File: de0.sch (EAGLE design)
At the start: 154 parts, among them IC1 PL2303SA__LF, J2 UX60SC-MB-5ST, Q1 BSH103,235, Q2 BSH103,235, Q3 BSH103,235, Q4 BSH103,235, Q5 BSH103,235, SW0 SS12SDP2, SW1 SS12SDP2, SW2 SS12SDP2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

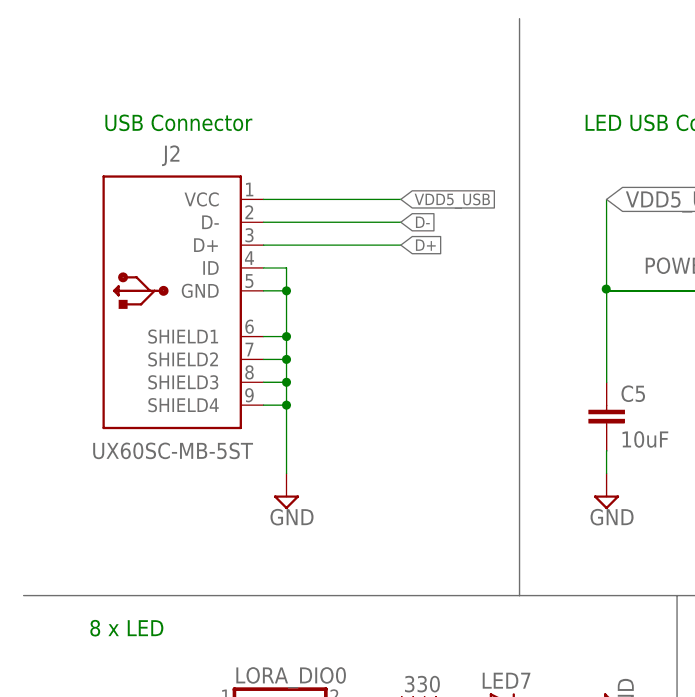
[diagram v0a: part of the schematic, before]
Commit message: change USB connector
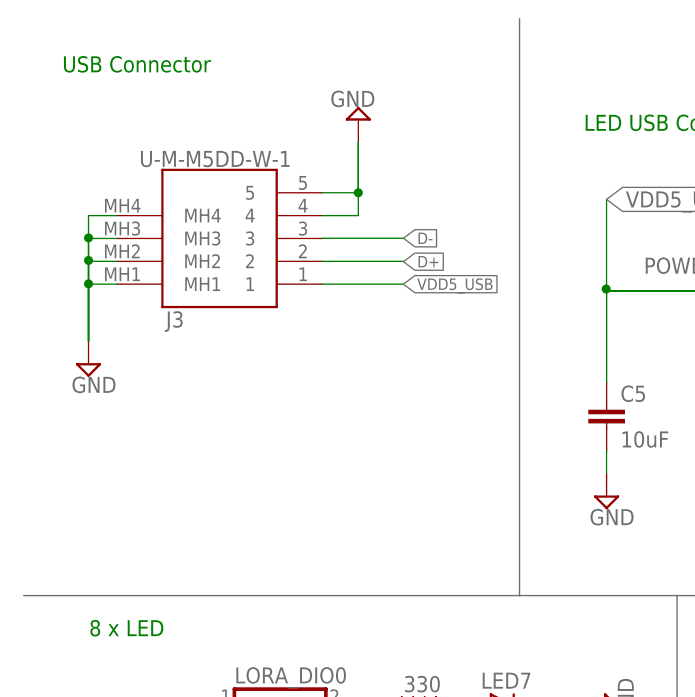
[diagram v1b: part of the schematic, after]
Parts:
- removed J2: UX60SC-MB-5ST, Connector_USB:UX60SC-MB-5ST
- added J3: U-M-M5DD-W-1, SamacSys_Parts:U-M-M5DD-W-1
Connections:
- net D+: now also J3.2; no longer J2.D+
- net D-: now also J3.3; no longer J2.D-
- net GND: now also J3.4, J3.5, J3.MH1, J3.MH2, J3.MH3, J3.MH4; no longer J2.GND, J2.ID, J2.SHIELD1, J2.SHIELD2, J2.SHIELD3, J2.SHIELD4
- net VDD5_USB: now also J3.1; no longer J2.VCC
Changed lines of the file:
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@@
 <part name="SV1" library="con-lsta" library_urn="urn:adsk.eagle:library:161" deviceset="FE10-1" device="" package3d_urn="urn:adsk.eagle:package:8192/1" value="SPI0"/>
 <part name="SV2" library="con-lsta" library_urn="urn:adsk.eagle:library:161" deviceset="FE10-1" device="" package3d_urn="urn:adsk.eagle:package:8192/1" value="SPI1"/>
-<part name="J2" library="Connector_USB" library_urn="urn:adsk.eagle:library:27510300" deviceset="UX60SC-MB-5ST" device="" package3d_urn="urn:adsk.eagle:package:27659496/1"/>
-<part name="SUPPLY18" library="supply2" library_urn="urn:adsk.eagle:library:372" deviceset="GND" device=""/>
 <part name="SUPPLY16" library="supply2" library_urn="urn:adsk.eagle:library:372" deviceset="GND" device=""/>
 <part name="R22" library="SparkFun-Resistors" library_urn="urn:adsk.eagle:library:532" deviceset="330OHM" device="-0603-1/10W-1%" package3d_urn="urn:adsk.eagle:package:39650/1" value="330"/>
@@
 <part name="H3" library="holes" library_urn="urn:adsk.eagle:library:237" deviceset="MOUNT-HOLE" device="3.3" package3d_urn="urn:adsk.eagle:package:14278/1"/>
 <part name="H4" library="holes" library_urn="urn:adsk.eagle:library:237" deviceset="MOUNT-HOLE" device="3.3" package3d_urn="urn:adsk.eagle:package:14278/1"/>
+<part name="J3" library="SamacSys_Parts" deviceset="U-M-M5DD-W-1" device=""/>
+<part name="SUPPLY43" library="supply2" library_urn="urn:adsk.eagle:library:372" deviceset="GND" device=""/>
+<part name="SUPPLY40" library="supply2" library_urn="urn:adsk.eagle:library:372" deviceset="GND" device=""/>
 </parts>
 <sheets>
 <sheet>
 <plain>
-<text x="-262.61" y="191.74" size="1.778" layer="91">USB Connector </text>
 <text x="-209.27" y="191.74" size="1.778" layer="91">LED USB Connector </text>
 <text x="-161.01" y="191.74" size="1.778" layer="91">USB TO UART</text>
@@
 <wire x1="-55.1" y1="-146.5" x2="198.8" y2="-146.5" width="0.1524" layer="95"/>
 <text x="-49.99" y="-62.18" size="1.778" layer="91">Power leds</text>
+<text x="-267.21" y="198.24" size="1.778" layer="91">USB Connector </text>
 </plain>
 <instances>
@@
 <attribute name="NAME" x="111.84" y="185.482" size="1.778" layer="95"/>
 </instance>
-<instance part="J2" gate="G$1" x="-254.99" y="173.96" smashed="yes" rot="MR0">
-<attribute name="NAME" x="-254.99" y="189.2" size="1.778" layer="95" rot="MR0" align="center"/>
-<attribute name="VALUE" x="-254.99" y="156.18" size="1.778" layer="96" rot="MR0" align="center"/>
-</instance>
-<instance part="SUPPLY18" gate="GND" x="-242.29" y="151.1" smashed="yes">
-<attribute name="VALUE" x="-244.195" y="147.925" size="1.778" layer="96"/>
-</instance>
 <instance part="SUPPLY16" gate="GND" x="-206.73" y="151.1" smashed="yes">
 <attribute name="VALUE" x="-208.635" y="147.925" size="1.778" layer="96"/>
@@
 <attribute name="VALUE" x="149.132" y="-38.2638" size="1.778" layer="96"/>
 </instance>
+<instance part="J3" gate="G$1" x="-238.3" y="174.7" smashed="yes" rot="R180">
+<attribute name="NAME" x="-253.65" y="170.78" size="1.778" layer="95" rot="R180" align="center-left"/>
+<attribute name="VALUE" x="-241.75" y="188.62" size="1.778" layer="96" rot="R180" align="center-left"/>
+</instance>
+<instance part="SUPPLY43" gate="GND" x="-264.29" y="165.8" smashed="yes">
+<attribute name="VALUE" x="-266.195" y="162.625" size="1.778" layer="96"/>
+</instance>
+<instance part="SUPPLY40" gate="GND" x="-234.31" y="193" smashed="yes" rot="R180">
+<attribute name="VALUE" x="-232.405" y="196.175" size="1.778" layer="96" rot="R180"/>
+</instance>
 </instances>
 <busses>
@@
 </segment>
 <segment>
-<pinref part="J2" gate="G$1" pin="SHIELD4"/>
-<wire x1="-244.83" y1="161.26" x2="-242.29" y2="161.26" width="0.1524" layer="91"/>
-<pinref part="J2" gate="G$1" pin="SHIELD3"/>
-<wire x1="-244.83" y1="163.8" x2="-242.29" y2="163.8" width="0.1524" layer="91"/>
-<pinref part="J2" gate="G$1" pin="SHIELD1"/>
-<wire x1="-244.83" y1="168.88" x2="-242.29" y2="168.88" width="0.1524" layer="91"/>
-<pinref part="J2" gate="G$1" pin="SHIELD2"/>
-<wire x1="-242.29" y1="168.88" x2="-242.29" y2="166.34" width="0.1524" layer="91"/>
-<wire x1="-242.29" y1="166.34" x2="-244.83" y2="166.34" width="0.1524" layer="91"/>
-<wire x1="-242.29" y1="163.8" x2="-242.29" y2="166.34" width="0.1524" layer="91"/>
-<junction x="-242.29" y="166.34"/>
-<wire x1="-242.29" y1="161.26" x2="-242.29" y2="163.8" width="0.1524" layer="91"/>
-<junction x="-242.29" y="163.8"/>
-<pinref part="J2" gate="G$1" pin="GND"/>
-<wire x1="-244.83" y1="173.96" x2="-242.29" y2="173.96" width="0.1524" layer="91"/>
-<wire x1="-242.29" y1="173.96" x2="-242.29" y2="168.88" width="0.1524" layer="91"/>
-<junction x="-242.29" y="168.88"/>
-<wire x1="-242.29" y1="161.26" x2="-242.29" y2="153.64" width="0.1524" layer="91"/>
-<junction x="-242.29" y="161.26"/>
-<pinref part="SUPPLY18" gate="GND" pin="GND"/>
-<pinref part="J2" gate="G$1" pin="ID"/>
-<wire x1="-244.83" y1="176.5" x2="-242.29" y2="176.5" width="0.1524" layer="91"/>
-<wire x1="-242.29" y1="173.96" x2="-242.29" y2="176.5" width="0.1524" layer="91"/>
-<junction x="-242.29" y="173.96"/>
-</segment>
-<segment>
 <pinref part="R22" gate="G$1" pin="1"/>
 <pinref part="SUPPLY31" gate="GND" pin="GND"/>
@@
 <wire x1="159.2" y1="-120.56" x2="159.5" y2="-120.56" width="0.1524" layer="91"/>
 </segment>
+<segment>
+<pinref part="J3" gate="G$1" pin="MH4"/>
+<pinref part="SUPPLY43" gate="GND" pin="GND"/>
+<wire x1="-261.16" y1="182.32" x2="-264.29" y2="182.32" width="0.1524" layer="91"/>
+<wire x1="-264.29" y1="182.32" x2="-264.29" y2="168.34" width="0.1524" layer="91"/>
+<pinref part="J3" gate="G$1" pin="MH3"/>
+<wire x1="-261.16" y1="179.78" x2="-264.29" y2="179.78" width="0.1524" layer="91"/>
+<wire x1="-264.29" y1="179.78" x2="-264.29" y2="168.34" width="0.1524" layer="91"/>
+<junction x="-264.29" y="179.84"/>
+<pinref part="J3" gate="G$1" pin="MH2"/>
+<wire x1="-261.16" y1="177.24" x2="-264.29" y2="177.24" width="0.1524" layer="91"/>
+<wire x1="-264.29" y1="177.24" x2="-264.29" y2="168.34" width="0.1524" layer="91"/>
+<junction x="-264.29" y="177.34"/>
+<pinref part="J3" gate="G$1" pin="MH1"/>
+<wire x1="-261.16" y1="174.7" x2="-264.29" y2="174.7" width="0.1524" layer="91"/>
+<wire x1="-264.29" y1="174.7" x2="-264.29" y2="168.34" width="0.1524" layer="91"/>
+<junction x="-264.29" y="174.74"/>
+</segment>
+<segment>
+<pinref part="J3" gate="G$1" pin="4"/>
+<pinref part="SUPPLY40" gate="GND" pin="GND"/>
+<wire x1="-238.3" y1="182.32" x2="-234.31" y2="182.32" width="0.1524" layer="91"/>
+<wire x1="-234.31" y1="182.32" x2="-234.31" y2="190.46" width="0.1524" layer="91"/>
+<pinref part="J3" gate="G$1" pin="5"/>
+<wire x1="-238.3" y1="184.86" x2="-234.31" y2="184.86" width="0.1524" layer="91"/>
+<wire x1="-234.31" y1="184.86" x2="-234.31" y2="190.46" width="0.1524" layer="91"/>
+<junction x="-234.31" y="184.86"/>
+</segment>
 </net>
 <net name="LORA_RESET" class="0">
@@
 </segment>
 <segment>
-<pinref part="J2" gate="G$1" pin="VCC"/>
-<wire x1="-244.83" y1="184.12" x2="-229.59" y2="184.12" width="0.1524" layer="91"/>
-<label x="-229.59" y="184.12" size="1.27" layer="95" xref="yes"/>
-</segment>
-<segment>
 <pinref part="D9" gate="G$1" pin="A"/>
 <wire x1="-196.57" y1="173.96" x2="-206.73" y2="173.96" width="0.1524" layer="91"/>
@@
 <junction x="-206.77" y="174.16"/>
 </segment>
+<segment>
+<pinref part="J3" gate="G$1" pin="1"/>
+<wire x1="-238.3" y1="174.7" x2="-229.3" y2="174.7" width="0.1524" layer="91"/>
+<label x="-229.3" y="174.7" size="1.27" layer="95" xref="yes"/>
+</segment>
 </net>
 <net name="VO_FPGA_33" class="0">
@@
 <net name="D-" class="0">
 <segment>
-<pinref part="J2" gate="G$1" pin="D-"/>
-<wire x1="-244.83" y1="181.58" x2="-229.59" y2="181.58" width="0.1524" layer="91"/>
-<label x="-229.59" y="181.58" size="1.27" layer="95" xref="yes"/>
-</segment>
-<segment>
 <pinref part="R9" gate="G$1" pin="2"/>
 <wire x1="-44.17" y1="171.42" x2="-36.55" y2="171.42" width="0.1524" layer="91"/>
 <label x="-36.55" y="171.42" size="1.778" layer="95" xref="yes"/>
 </segment>
+<segment>
+<pinref part="J3" gate="G$1" pin="3"/>
+<wire x1="-238.3" y1="179.78" x2="-238.3" y2="179.8" width="0.1524" layer="91"/>
+<wire x1="-238.3" y1="179.8" x2="-229.3" y2="179.8" width="0.1524" layer="91"/>
+<label x="-229.3" y="179.8" size="1.27" layer="95" xref="yes"/>
+</segment>
 </net>
 <net name="N$1" class="0">
@@
 <net name="D+" class="0">
 <segment>
-<pinref part="J2" gate="G$1" pin="D+"/>
-<wire x1="-244.83" y1="179.04" x2="-229.59" y2="179.04" width="0.1524" layer="91"/>
-<label x="-229.59" y="179.04" size="1.27" layer="95" xref="yes"/>
-</segment>
-<segment>
 <pinref part="R10" gate="G$1" pin="2"/>
 <wire x1="-44.17" y1="163.8" x2="-41.63" y2="163.8" width="0.1524" layer="91"/>
@@
 <junction x="-41.63" y="163.8"/>
 </segment>
+<segment>
+<pinref part="J3" gate="G$1" pin="2"/>
+<wire x1="-238.3" y1="177.24" x2="-229.3" y2="177.24" width="0.1524" layer="91"/>
+<label x="-229.3" y="177.2" size="1.27" layer="95" xref="yes"/>
+</segment>
 </net>
